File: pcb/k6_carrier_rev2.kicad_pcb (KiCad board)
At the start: 2 copper layers, 100 x 80 mm, 32 parts, among them J1 12V_DC, J2 48V_DC, SW1 RING, SW2 CANCEL, SW3 RESET, SW4 MODE, T1 600R_XFMR, U1 PC817, U2 L293D

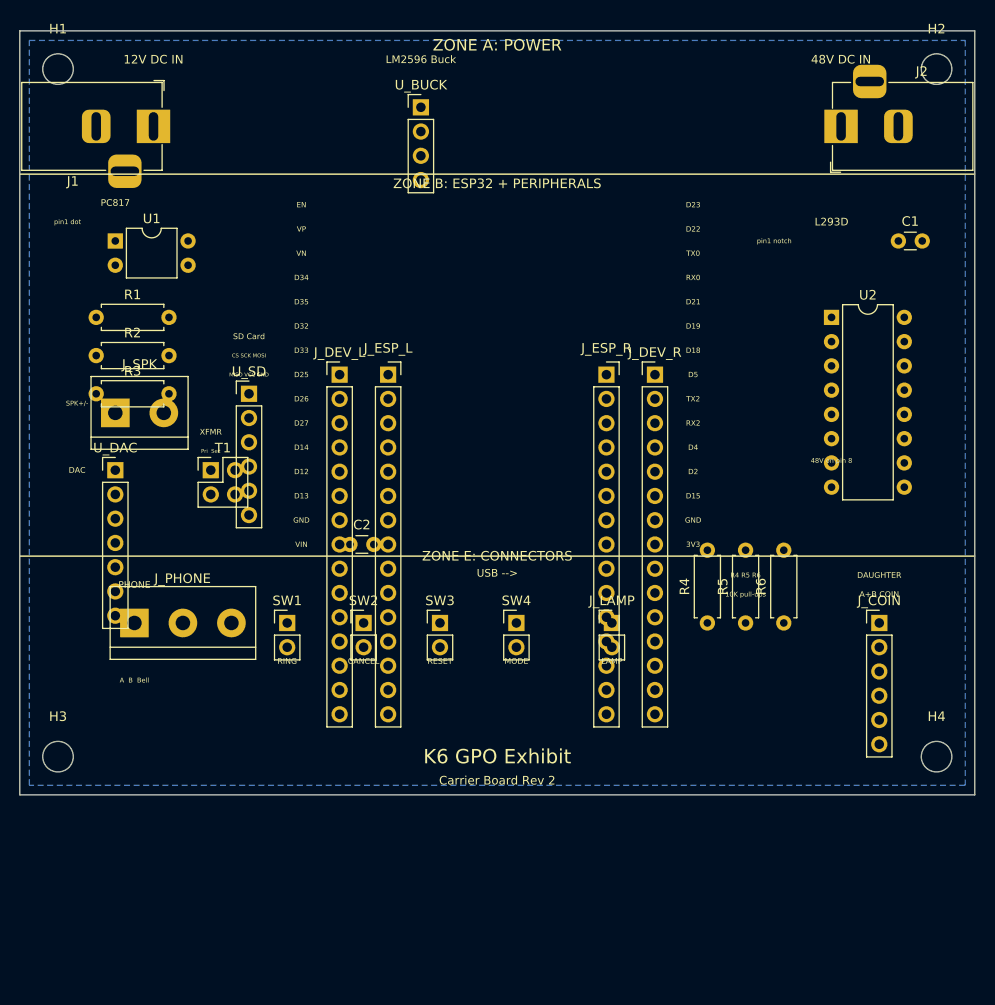
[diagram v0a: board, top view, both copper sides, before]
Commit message: feat: add 5x 1N4007 protection diodes, increase board to 100x100mm
- D1: anti-parallel across PC817 LED, clamps 48V reverse voltage to 0.7V
- D2-D5: overvoltage clamps on transformer primary (DAC_LP/DAC_LN to +5V and GND)
- Board increased from 100x80mm to 100x100mm for new Zone D (protection diodes)
- Zone layout: A (power) / B (ESP32+peripherals) / D (protection) / E (connectors)
- BOM and schematic updated with diode specs, interconnect table, and layout rules
- 158 total pads, 140 assigned to nets, 18 intentionally unassigned

Co-Authored-By: Devin AI <158243242+devin-ai-integration[bot]@users.noreply.github.com>
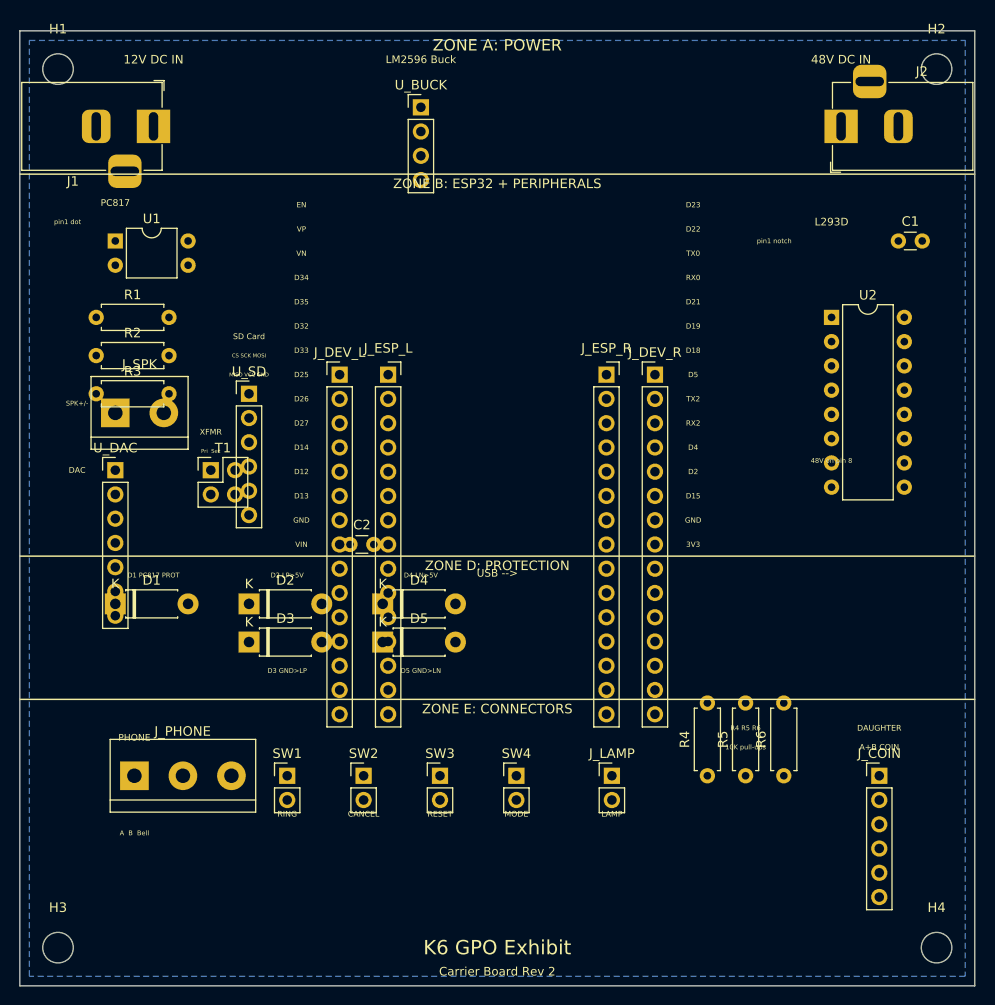
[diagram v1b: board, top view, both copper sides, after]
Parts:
- added D1: 1N4007, D_DO-41_SOD81_P7.62mm_Horizontal, F.Cu at (110.0, 110.0)
- added D2: 1N4007, D_DO-41_SOD81_P7.62mm_Horizontal, F.Cu at (124.0, 110.0)
- added D3: 1N4007, D_DO-41_SOD81_P7.62mm_Horizontal, F.Cu at (124.0, 114.0)
- added D4: 1N4007, D_DO-41_SOD81_P7.62mm_Horizontal, F.Cu at (138.0, 110.0)
- added D5: 1N4007, D_DO-41_SOD81_P7.62mm_Horizontal, F.Cu at (138.0, 114.0)
- moved H3 20.0 mm to (104.0, 146.0)
- moved H4 20.0 mm to (196.0, 146.0)
- moved J_COIN 16.0 mm to (190.0, 128.0)
- moved J_LAMP 16.0 mm to (162.0, 128.0)
- moved J_PHONE 16.0 mm to (112.0, 128.0)
- moved R4 16.0 mm to (172.0, 128.0)
- moved R5 16.0 mm to (176.0, 128.0)
- moved R6 16.0 mm to (180.0, 128.0)
- moved SW1 16.0 mm to (128.0, 128.0)
- moved SW2 16.0 mm to (136.0, 128.0)
- moved SW3 16.0 mm to (144.0, 128.0)
- moved SW4 16.0 mm to (152.0, 128.0)
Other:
- board size 100 x 80 mm -> 100 x 100 mm
- board text added: "D1 PC817 PROT"
- board text added: "D2 LP>5V"
- board text added: "D3 GND>LP"
- board text added: "D4 LN>5V"
- board text added: "D5 GND>LN"
- board text added: "ZONE D: PROTECTION"

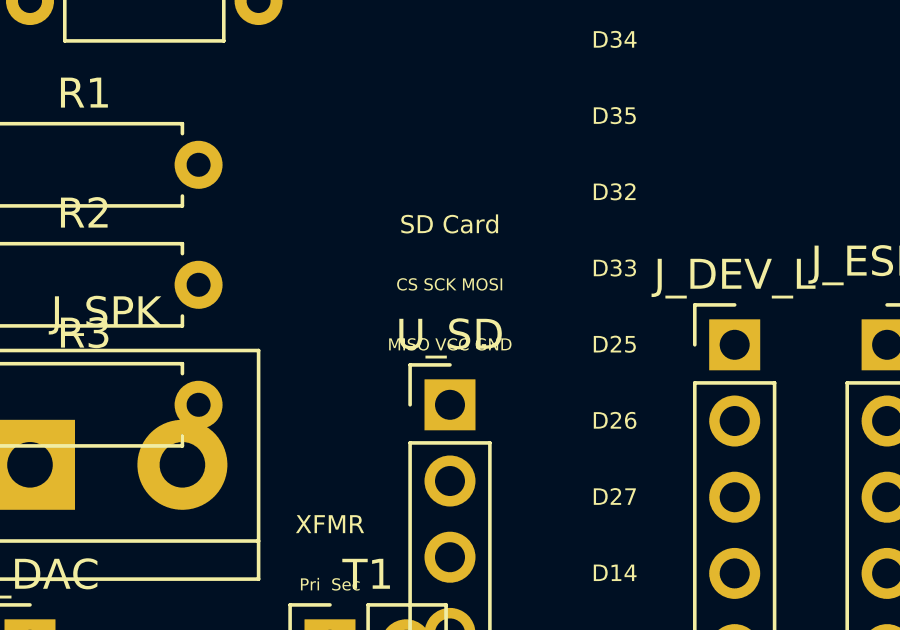
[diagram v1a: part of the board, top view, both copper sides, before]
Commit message: fix: update SD card module pin order to 3V3 CS MOSI CLK MISO GND
Matches the user's actual breakout board pin sequence (previously
CS SCK MOSI MISO VCC GND). Silkscreen labels and net assignments
updated accordingly.

Co-Authored-By: Devin AI <158243242+devin-ai-integration[bot]@users.noreply.github.com>
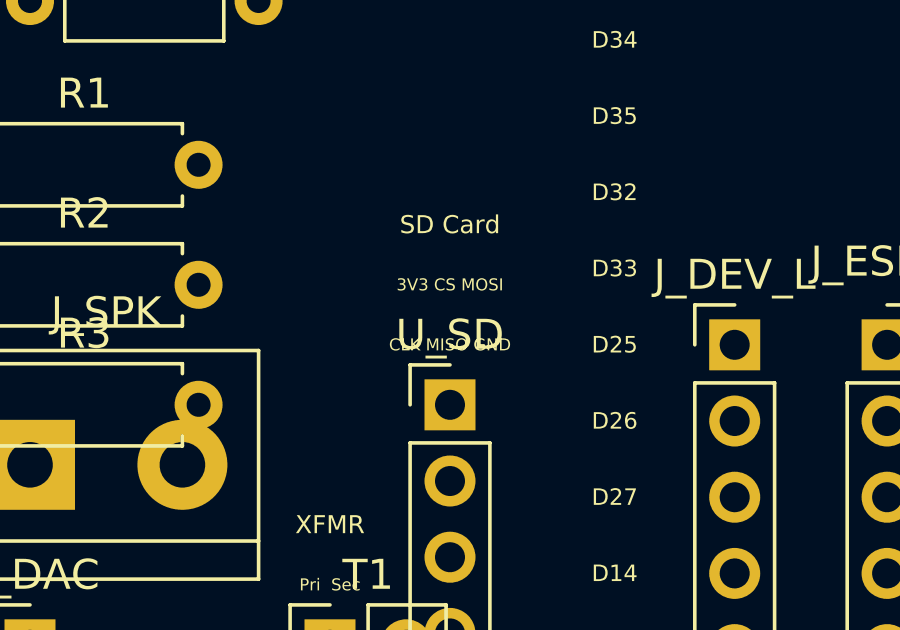
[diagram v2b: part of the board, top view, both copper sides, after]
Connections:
- U_SD pad 1: GPIO5 -> +3V3
- U_SD pad 2: GPIO18 -> GPIO5
- U_SD pad 4: GPIO19 -> GPIO18
- U_SD pad 5: +3V3 -> GPIO19
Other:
- board text added: "3V3 CS MOSI"
- board text added: "CLK MISO GND"
- board text removed: "CS SCK MOSI"
- board text removed: "MISO VCC GND"
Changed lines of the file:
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@@
     (fp_line (start 1.27 13.97) (end -1.27 13.97) (layer "F.Fab") (width 0.1))
     (pad "1" thru_hole rect (at 0 0) (size 1.7 1.7) (drill 1) (layers *.Cu *.Mask)
+      (net 3 "+3V3"))
+    (pad "2" thru_hole oval (at 0 2.54) (size 1.7 1.7) (drill 1) (layers *.Cu *.Mask)
       (net 12 "GPIO5"))
-    (pad "2" thru_hole oval (at 0 2.54) (size 1.7 1.7) (drill 1) (layers *.Cu *.Mask)
-      (net 15 "GPIO18"))
     (pad "3" thru_hole oval (at 0 5.08) (size 1.7 1.7) (drill 1) (layers *.Cu *.Mask)
       (net 13 "GPIO23"))
     (pad "4" thru_hole oval (at 0 7.62) (size 1.7 1.7) (drill 1) (layers *.Cu *.Mask)
+      (net 15 "GPIO18"))
+    (pad "5" thru_hole oval (at 0 10.16) (size 1.7 1.7) (drill 1) (layers *.Cu *.Mask)
       (net 14 "GPIO19"))
-    (pad "5" thru_hole oval (at 0 10.16) (size 1.7 1.7) (drill 1) (layers *.Cu *.Mask)
-      (net 3 "+3V3"))
     (pad "6" thru_hole oval (at 0 12.7) (size 1.7 1.7) (drill 1) (layers *.Cu *.Mask)
       (net 1 "GND"))
@@
     (effects (font (size 0.55 0.55) (thickness 0.08)))
   )
-  (gr_text "MISO VCC GND" (at 124 86) (layer "F.SilkS")
+  (gr_text "CLK MISO GND" (at 124 86) (layer "F.SilkS")
     (effects (font (size 0.4 0.4) (thickness 0.06)))
   )
@@
     (effects (font (size 0.6 0.6) (thickness 0.1)))
   )
-  (gr_text "CS SCK MOSI" (at 124 84) (layer "F.SilkS")
+  (gr_text "3V3 CS MOSI" (at 124 84) (layer "F.SilkS")
     (effects (font (size 0.4 0.4) (thickness 0.06)))
   )

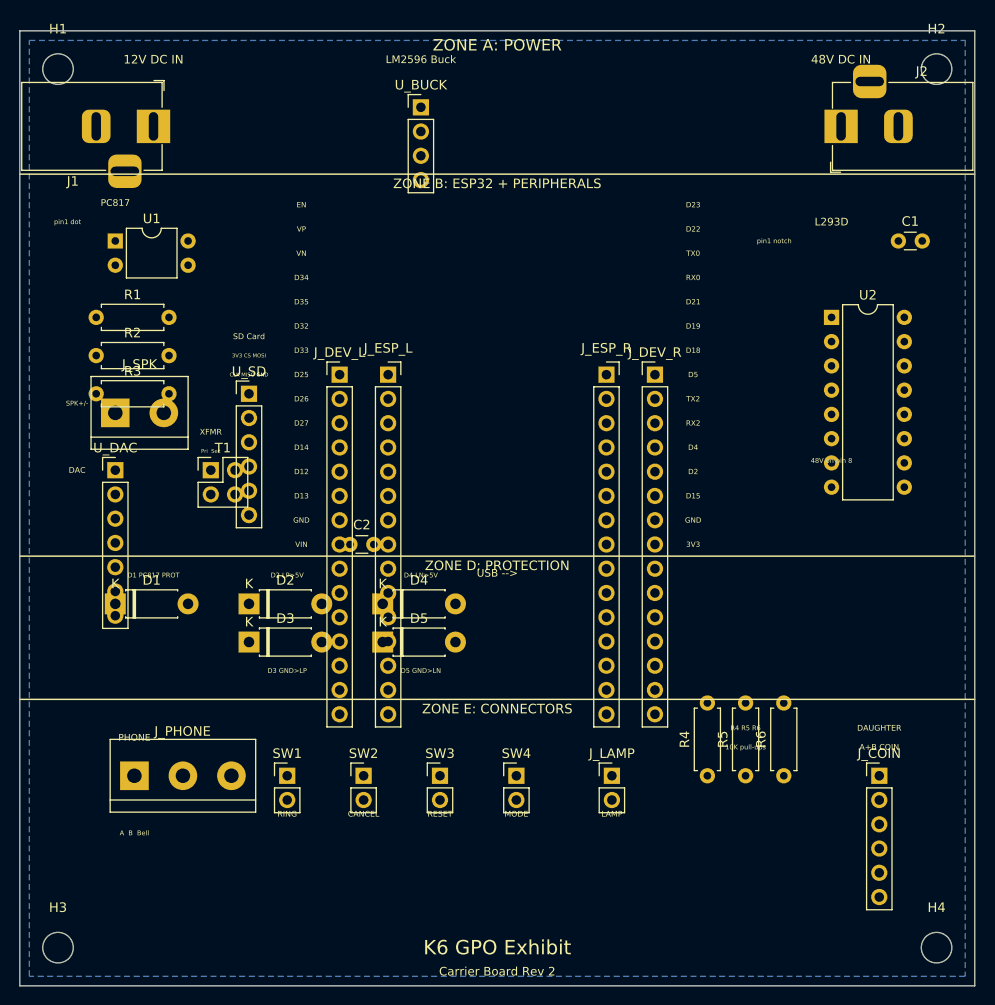
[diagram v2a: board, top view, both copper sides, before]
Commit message: pcb: replace with routed board files, remove pre-generated gerbers
- Carrier board: replaced with user's routed k6_carrier_rev2 PCB
- Daughter board: replaced with user's routed k6_coinbox_daughter PCB
- Removed pcb/gerbers/ directory (users should export their own
  gerbers from KiCad with their preferred fabricator settings)
- Updated docs to reference KiCad export instead of pre-generated files

Co-Authored-By: Devin AI <158243242+devin-ai-integration[bot]@users.noreply.github.com>
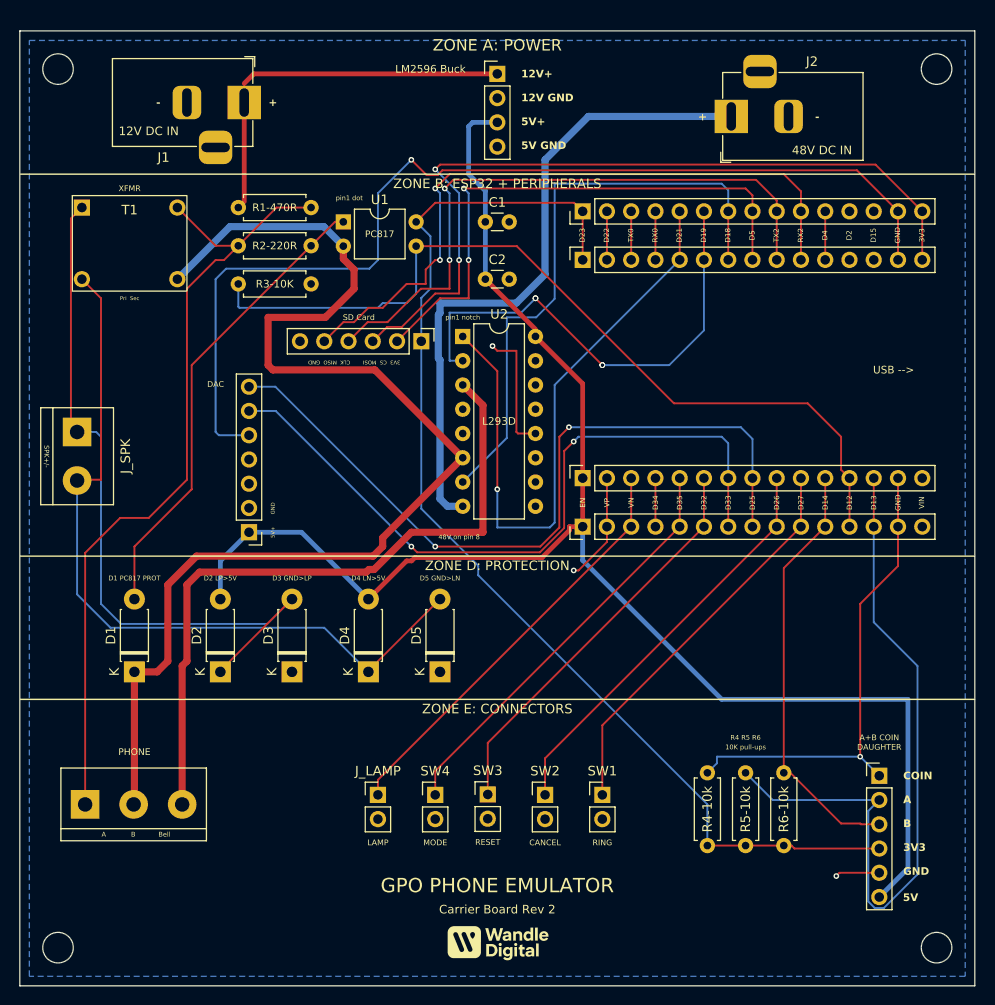
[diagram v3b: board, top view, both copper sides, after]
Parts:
- R1-470R: renamed from R1; value 470R_1W -> R2-470R
- R2-220R: renamed from R2; value 220R -> R3-220R
- moved C1 43.3 mm to (148.8, 70.0)
- moved U2 38.7 mm to (146.4, 82.0)
- moved SW1 33.1 mm to (161.0, 130.0)
- moved C2 31.2 mm to (148.8, 76.0)
- moved J_DEV_L 30.0 mm to (158.9, 101.9), turned to 90 degrees
- moved T1 25.2 mm to (111.5, 72.2)
- moved J_LAMP 24.6 mm to (137.5, 130.0)
- moved U1 24.0 mm to (133.9, 70.0)
- moved J_ESP_L 23.1 mm to (158.9, 96.8), turned to 90 degrees
- moved SW2 19.1 mm to (155.0, 130.0)
- moved U_SD 18.9 mm to (142.0, 82.5), turned to -90 degrees
- moved R1-470R 18.8 mm to (122.9, 68.5)
- moved R2-220R 18.8 mm to (122.9, 72.5)
- moved R3-10K 18.8 mm to (122.9, 76.5)
- moved J_DEV_R 18.7 mm to (158.9, 68.9), turned to 90 degrees
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- renumbered R3 to R3-10K, R4 to R4-10k, R5 to R5-10k, R6 to R6-10k
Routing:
- net +5V: track 0.00 -> 165.0 mm
- net LINE_B: track 0.00 -> 127.9 mm
- net +3V3: track 0.00 -> 120.6 mm
- net GPIO22: track 0.00 -> 108.1 mm, vias 0 -> 1
- net GPIO34: track 0.00 -> 89.2 mm
- net LINE_A: track 0.00 -> 84.7 mm
- net GPIO23: track 0.00 -> 83.5 mm, vias 0 -> 2
- net DAC_LN: track 0.00 -> 80.9 mm
- net GPIO25: track 0.00 -> 80.1 mm, vias 0 -> 2
- net DAC_LP: track 0.00 -> 77.1 mm
- net GPIO39: track 0.00 -> 76.6 mm
- net GPIO26: track 0.00 -> 75.1 mm, vias 0 -> 2
- net BELL: track 0.00 -> 72.8 mm
- net GPIO19: track 0.00 -> 71.1 mm, vias 0 -> 2
- net +48V: track 0.00 -> 69.0 mm
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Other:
- board text added: "+"
- board text added: "-"
- board text added: "12V GND"
- board text added: "12V+"
- board text added: "5V"
- board text added: "5V GND"
- board text added: "5V+"
- board text added: "A"
- board text added: "B"
- board text added: "COIN"
- board text added: "GPO PHONE EMULATOR"
- board text removed: "K6 GPO Exhibit"

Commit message: pcb: update carrier board with F.Cu ground pour
Co-Authored-By: Devin AI <158243242+devin-ai-integration[bot]@users.noreply.github.com>
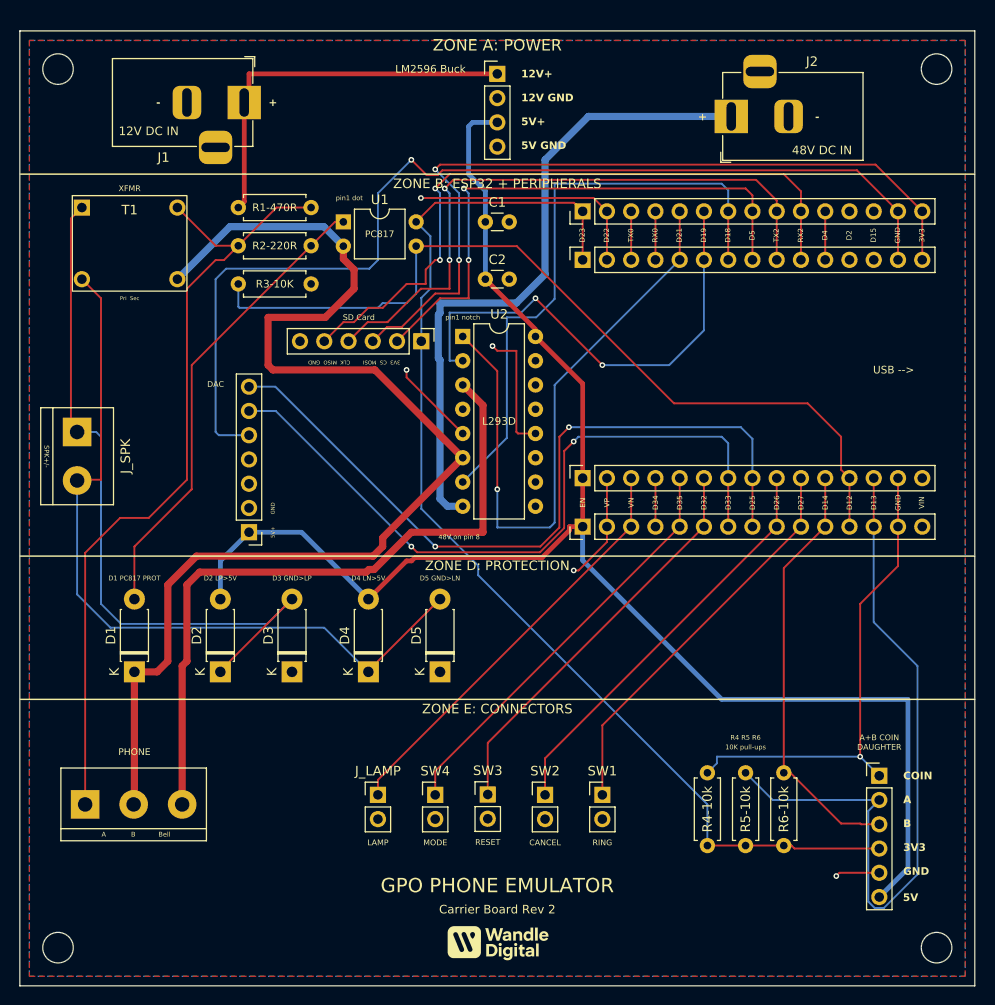
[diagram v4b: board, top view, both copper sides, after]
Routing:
- net GND: track 34.4 -> 63.5 mm, vias 3 -> 5
- net GPIO16: vias 4 -> 2
- added copper zone on F.Cu, net GND
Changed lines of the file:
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@@
+	)
+	(segment
+		(start 160.085 67.5)
+		(end 142 67.5)
+		(width 0.2)
+		(layer "F.Cu")
+		(net "GND")
+	)
+	(segment
+		(start 146.38 92.16)
+		(end 140.5 86.28)
+		(width 0.2)
+		(layer "F.Cu")
+		(net "GND")
 	)
 	(segment
@@
 	)
 	(segment
+		(start 161.48 68.895)
+		(end 160.085 67.5)
+		(width 0.2)
+		(layer "F.Cu")
+		(net "GND")
+	)
+	(segment
 		(start 190 138.16)
 		(end 185.84 138.16)
@@
 		(start 152 83.5)
 		(end 150 83.5)
+		(width 0.2)
+		(layer "F.Cu")
+		(net "GND")
+	)
+	(segment
+		(start 140.5 86.28)
+		(end 140.5 85.5)
 		(width 0.2)
 		(layer "F.Cu")
@@
 	)
 	(via
+		(at 140.5 85.5)
+		(size 0.6)
+		(drill 0.3)
+		(layers "F.Cu" "B.Cu")
+		(net "GND")
+	)
+	(via
 		(at 185.5 138.5)
+		(size 0.6)
+		(drill 0.3)
+		(layers "F.Cu" "B.Cu")
+		(net "GND")
+	)
+	(via
+		(at 142 67.5)
 		(size 0.6)
 		(drill 0.3)
@@
 	)
 	(segment
-		(start 123.5 55.5)
-		(end 124.5 54.5)
+		(start 124 54.5)
+		(end 124 57)
 		(width 0.5)
 		(layer "F.Cu")
@@
 	)
 	(segment
-		(start 124.5 54.5)
-		(end 150 54.5)
-		(width 0.5)
-		(layer "F.Cu")
-		(net "+12V")
-	)
-	(segment
-		(start 123.5 57.5)
-		(end 123.5 55.5)
-		(width 0.2)
+		(start 124 57)
+		(end 123.5 57.5)
+		(width 0.5)
 		(layer "F.Cu")
 		(net "+12V")
@@
 		(start 123.5 67.88)
 		(end 122.88 68.5)
-		(width 0.2)
+		(width 0.5)
+		(layer "F.Cu")
+		(net "+12V")
+	)
+	(segment
+		(start 150 54.5)
+		(end 124 54.5)
+		(width 0.5)
 		(layer "F.Cu")
 		(net "+12V")
@@
 		(net "GPIO16")
 	)
-	(via
-		(at 154 78)
-		(size 0.6)
-		(drill 0.3)
-		(layers "F.Cu" "B.Cu")
-		(net "GPIO16")
-	)
-	(via
-		(at 161 85)
-		(size 0.6)
-		(drill 0.3)
-		(layers "F.Cu" "B.Cu")
-		(net "GPIO16")
-	)
 	(segment
 		(start 161 85)
@@
 	)
 	(zone
+		(net "GND")
+		(layer "F.Cu")
+		(hatch edge 0.5)
+		(priority 1)
+		(connect_pads
+			(clearance 0.5)
+		)
+		(min_thickness 0.25)
+		(fill yes
+			(thermal_gap 0.5)
+			(thermal_bridge_width 0.5)
+			(island_removal_mode 0)
+		)
+		(polygon
+			(pts
+				(xy 101 51) (xy 101 149) (xy 199 149) (xy 199 51)
+			)
+		)
+	)
+	(zone
